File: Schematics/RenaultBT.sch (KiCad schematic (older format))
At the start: 3 parts, among them J1 PowerSupply, J2 SPDIF_Output, J3 HU_CDC_Interface

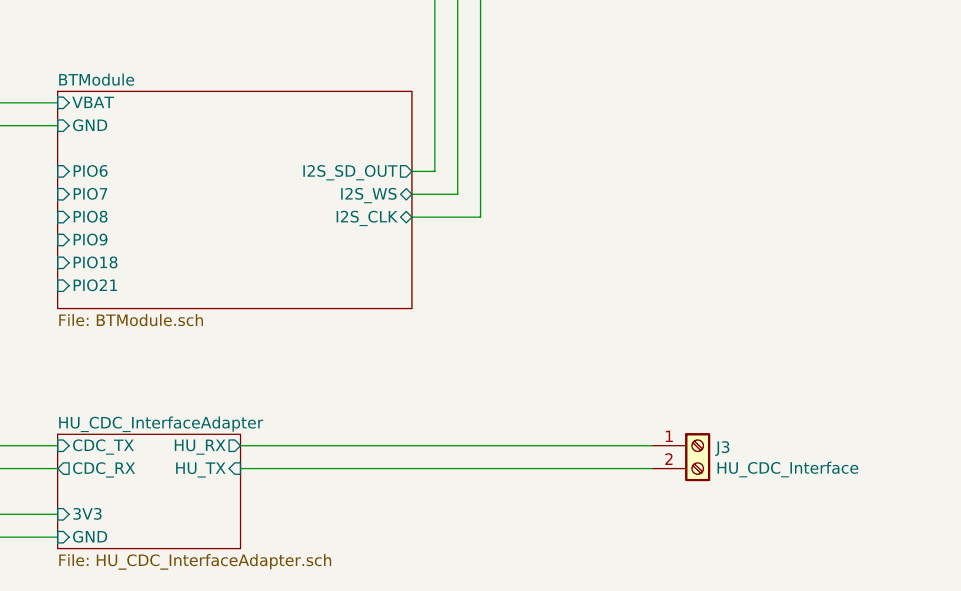
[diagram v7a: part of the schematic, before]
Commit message: Fixed CDC interface schematic; Fixed SPDIF output interface schematic; Added screw terminals; Modified PCB design
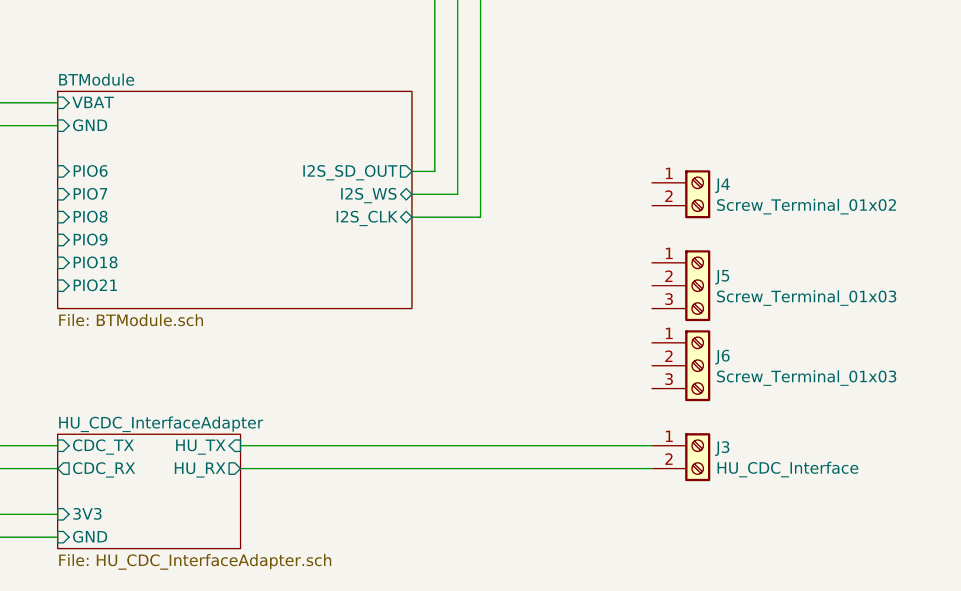
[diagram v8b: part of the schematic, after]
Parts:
- added J4: Screw_Terminal_01x02, ScrewTerminal:ScrewTerminal_2, symbol Connector:Screw_Terminal_01x02
- added J5, J6: Screw_Terminal_01x03, ScrewTerminal:ScrewTerminal_3, symbol Connector:Screw_Terminal_01x03
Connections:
- net HU_CDC_InterfaceAdapter/HU_RX: now also J3.2 (Pin_2); no longer J3.1 (Pin_1)
- net HU_CDC_InterfaceAdapter/HU_TX: now also J3.1 (Pin_1); no longer J3.2 (Pin_2)
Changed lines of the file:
@@
 F2 "GND" I L 4950 4850 50
 F3 "CDC_TX" I L 4950 4450 50
-F4 "HU_RX" O R 5750 4450 50
-F5 "HU_TX" I R 5750 4550 50
+F4 "HU_RX" O R 5750 4550 50
+F5 "HU_TX" I R 5750 4450 50
 F6 "CDC_RX" O L 4950 4550 50
 F7 "3V3" I L 4950 4750 50
@@
 Wire Wire Line
 	1600 1800 1050 1800
+$Comp
+L Connector:Screw_Terminal_01x03 J6
+U 1 1 5D463BB8
+P 7750 4100
+F 0 "J6" H 7830 4142 50  0000 L CNN
+F 1 "Screw_Terminal_01x03" H 7830 4051 50  0000 L CNN
+F 2 "ScrewTerminal:ScrewTerminal_3" H 7750 4100 50  0001 C CNN
+F 3 "~" H 7750 4100 50  0001 C CNN
+	1    7750 4100
+	1    0    0    -1
+$EndComp
+$Comp
+L Connector:Screw_Terminal_01x03 J5
+U 1 1 5D463C02
+P 7750 3750
+F 0 "J5" H 7830 3792 50  0000 L CNN
+F 1 "Screw_Terminal_01x03" H 7830 3701 50  0000 L CNN
+F 2 "ScrewTerminal:ScrewTerminal_3" H 7750 3750 50  0001 C CNN
+F 3 "~" H 7750 3750 50  0001 C CNN
+	1    7750 3750
+	1    0    0    -1
+$EndComp
+$Comp
+L Connector:Screw_Terminal_01x02 J4
+U 1 1 5D463CE6
+P 7750 3300
+F 0 "J4" H 7830 3292 50  0000 L CNN
+F 1 "Screw_Terminal_01x02" H 7830 3201 50  0000 L CNN
+F 2 "ScrewTerminal:ScrewTerminal_2" H 7750 3300 50  0001 C CNN
+F 3 "~" H 7750 3300 50  0001 C CNN
+	1    7750 3300
+	1    0    0    -1
+$EndComp
 $EndSCHEMATC
